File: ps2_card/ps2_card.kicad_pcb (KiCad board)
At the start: 2 copper layers, 100 x 70 mm, 16 parts, among them J1 Conn1, J2 Mouse, J3 Keyboard, U1 HT6542B, U2 74HCT04

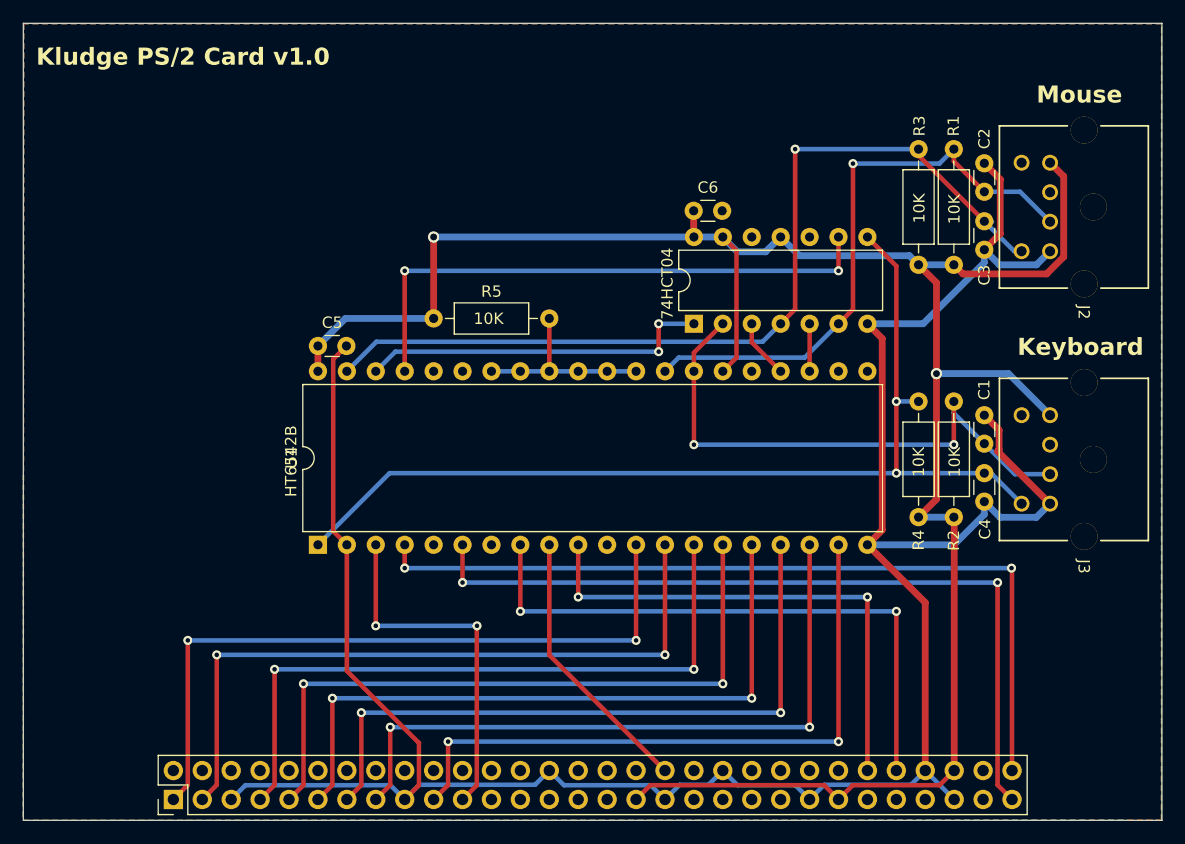
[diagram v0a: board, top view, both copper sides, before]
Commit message: Fixed mirrored PS/2 port footprint.
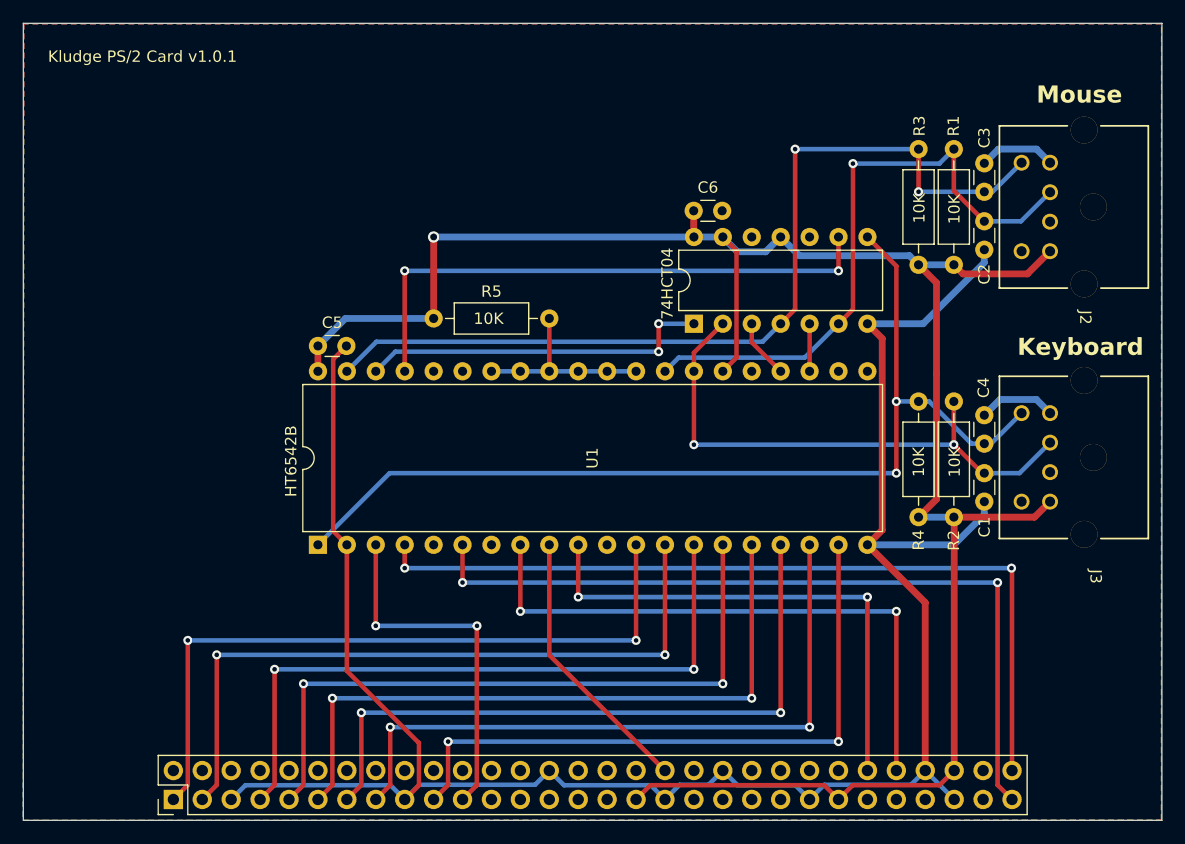
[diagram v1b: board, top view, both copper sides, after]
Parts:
- moved C1 2.59 mm to (175.8, 113.4), turned to -90 degrees
- moved C2 2.59 mm to (175.8, 91.3), turned to -90 degrees
- moved C3 2.59 mm to (175.8, 88.7), turned to 90 degrees
- moved C4 2.59 mm to (175.8, 110.9), turned to 90 degrees
- moved J2 1.49 mm to (182.6, 87.2)
- moved J3 1.37 mm to (182.6, 109.2)
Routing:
- net GND: track 216.0 -> 197.0 mm
- net VCC: track 193.4 -> 181.2 mm, vias 2 -> 1
- net MOUSE_DATA: track 52.7 -> 56.0 mm
- net KB_CLK: track 90.6 -> 89.4 mm
- net MOUSE_CLK: vias 1 -> 2
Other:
- board text added: "Kludge PS/2 Card v1.0.1"
- board text removed: "Kludge PS/2 Card v1.0"

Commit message: Replaced 74xx04's with 74xx06's in order for the ps/2 device to be able to properly send data/clock
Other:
- board text added: "74HCT06"
- board text removed: "74HCT04"
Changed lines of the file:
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@@
 	(net 61 "unconnected-(J2-Pad2)")
 	(net 62 "unconnected-(J2-Pad6)")
-	(net 63 "unconnected-(J3-Pad6)_1")
+	(net 63 "unconnected-(J3-Pad6)")
 	(net 64 "unconnected-(J3-Pad2)")
 	(net 65 "Net-(U1-KBDO)")
@@
 			(layers "*.Cu" "*.Mask")
 			(remove_unused_layers no)
-			(net 63 "unconnected-(J3-Pad6)_1")
+			(net 63 "unconnected-(J3-Pad6)")
 			(pintype "passive+no_connect")
 		)
@@
 		)
 	)
-	(gr_text "74HCT04"
+	(gr_text "74HCT06"
 		(at 148.55 99.954524 90)
 		(layer "F.SilkS")

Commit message: Replaced 74xx04's with 74xx06's in order for the ps/2 device to be able to properly send data/clock
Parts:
- U2: value 74HCT04 -> 74LS06
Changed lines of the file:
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@@
 			)
 		)
-		(property "Value" "74HCT04"
+		(property "Value" "74LS06"
 			(at 3.81 17.5246 90)
 			(layer "F.Fab")
@@
 			)
 		)
-		(property "Datasheet" "https://assets.nexperia.com/documents/data-sheet/74HC_HCT04.pdf"
+		(property "Datasheet" "http://www.ti.com/lit/gpn/sn74LS06"
 			(at 0 0 90)
 			(unlocked yes)
@@
 			)
 		)
-		(property "Description" "Hex Inverter"
+		(property "Description" "Inverter Open Collect"
 			(at 0 0 90)
 			(unlocked yes)
@@
 			)
 		)
-		(property ki_fp_filters "DIP*W7.62mm* SSOP?14* TSSOP?14*")
+		(property ki_fp_filters "DIP*W7.62mm*")
 		(sheetname "Root")
 		(sheetfile "ps2_card.kicad_sch")
@@
 			(remove_unused_layers no)
 			(net 56 "KB_DATA")
-			(pintype "output")
+			(pintype "open_collector")
 		)
 		(pad "3" thru_hole oval
@@
 			(remove_unused_layers no)
 			(net 58 "MOUSE_CLK")
-			(pintype "output")
+			(pintype "open_collector")
 		)
 		(pad "5" thru_hole oval
@@
 			(remove_unused_layers no)
 			(net 57 "MOUSE_DATA")
-			(pintype "output")
+			(pintype "open_collector")
 		)
 		(pad "7" thru_hole oval
@@
 			(remove_unused_layers no)
 			(net 59 "KB_CLK")
-			(pintype "output")
+			(pintype "open_collector")
 		)
 		(pad "9" thru_hole oval
@@
 			(remove_unused_layers no)
 			(net 70 "unconnected-(U2-Pad10)")
-			(pintype "output+no_connect")
+			(pintype "open_collector+no_connect")
 		)
 		(pad "11" thru_hole oval
@@
 			(remove_unused_layers no)
 			(net 69 "unconnected-(U2-Pad12)")
-			(pintype "output+no_connect")
+			(pintype "open_collector+no_connect")
 		)
 		(pad "13" thru_hole oval
